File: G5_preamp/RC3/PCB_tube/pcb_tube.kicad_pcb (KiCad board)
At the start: 2 copper layers, 100 x 47 mm, 31 parts, among them J1 PSU_TUBE, J2 PCB_TUBE, J3 OT

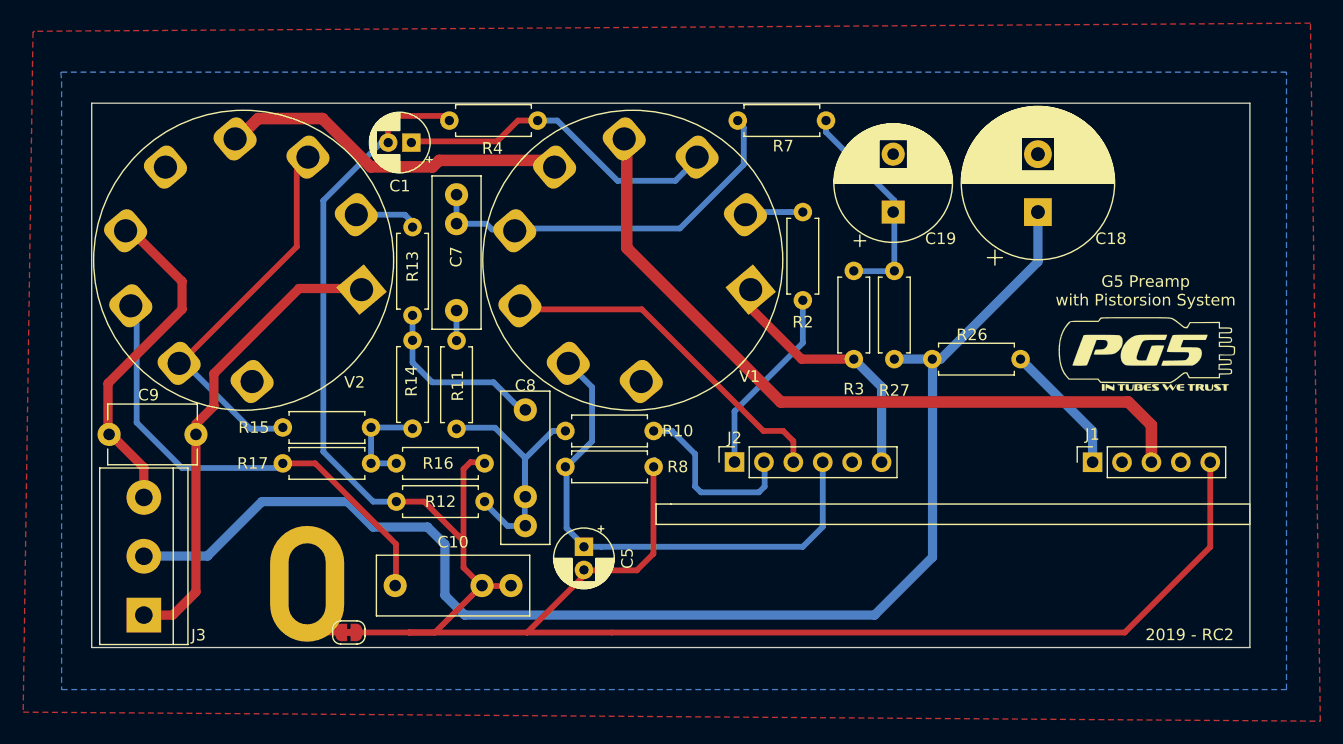
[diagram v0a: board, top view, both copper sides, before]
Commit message: RC3 update
Cathode Cap change 3d models and place (pcb-main)
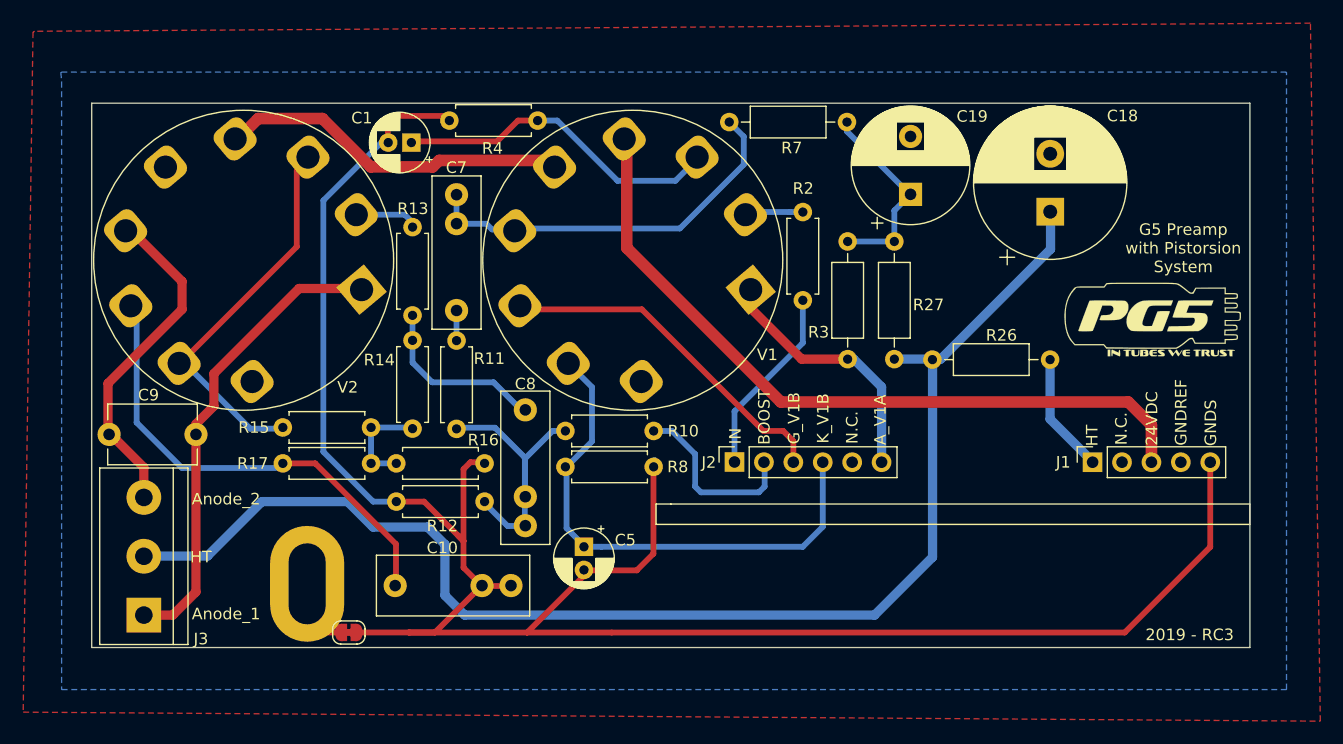
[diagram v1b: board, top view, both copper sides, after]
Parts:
- R26, R27, R3, R7: footprint Resistor_THT:R_Axial_DIN0207_L6.3mm_D2.5mm_P7.62mm_Horizontal -> Resistor_THT:R_Axial_DIN0207_L6.3mm_D2.5mm_P10.16mm_Horizontal
- moved REF** 3.01 mm to (121.6, 71.4)
- moved R3 2.59 mm to (95.3, 64.9)
- moved R26 2.55 mm to (112.8, 75.1)
- moved C19 2.14 mm to (100.7, 60.9)
- moved R7 1.81 mm to (95.2, 54.6)
- moved C18 1.06 mm to (112.8, 62.4)
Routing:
- net Net-(C19-Pad1): track 19.4 -> 17.2 mm
- net /HT2: track 11.5 -> 10.4 mm
- net /A+: track 115.9 -> 116.5 mm
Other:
- board text added: "2019 - RC3"
- board text added: "24VDC"
- board text added: "A_V1A"
- board text added: "Anode_1"
- board text added: "Anode_2"
- board text added: "BOOST"
- board text added: "GNDREF"
- board text added: "GNDS"
- board text added: "G_V1B"
- board text added: "HT"
- board text added: "IN"
- board text added: "K_V1B"
- board text added: "N.C."
- board text removed: "2019 - RC2"

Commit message: RC3 multivoltage
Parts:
- removed REF**: PG5_Logo_15mm_SilkScreen, Symbol:PG5_Logo_15mm_SilkScreen
- added J4: Conn_02x02_Odd_Even, Connector_PinHeader_2.54mm:PinHeader_1x04_P2.54mm_Vertical, F.Cu at (64.5, 56.5)
- added R20: 10k, Resistor_THT:R_Axial_DIN0207_L6.3mm_D2.5mm_P7.62mm_Horizontal, F.Cu at (81.8, 95.7)
- J2: footprint Connector_PinSocket_2.54mm:PinSocket_1x06_P2.54mm_Vertical -> Connector_PinHeader_2.54mm:PinHeader_1x07_P2.54mm_Vertical
- moved C1 38.3 mm to (95.9, 56.8), turned to 90 degrees
- moved R4 15.9 mm to (84.4, 54.8), turned to 0 degrees
- moved R7 7.64 mm to (100.6, 60.0)
- moved C19 6.21 mm to (106.9, 60.8)
- moved C18 6.18 mm to (118.9, 62.3)
- moved R26 1.15 mm to (113.9, 75.1)
- moved R2 0.73 mm to (91.5, 63.1)
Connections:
- C10 pad 2: GNDS -> /NFB
- J1 pad 2: Net-(J1-Pad2) -> (no net)
- J1 pad 3: /24VDC -> /HEATER
- J2 pad 5: Net-(J2-Pad5) -> /NFB
- J2 pad 6: /A_V1A -> (no net)
- R16 pad 2: GNDS -> /NFB
- V1 pad 4: /24VDC -> /HEATER1
- V1 pad 9: Net-(V1-Pad9) -> (no net)
- V2 pad 9: Net-(V2-Pad9) -> (no net)
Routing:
- net /HEATER: track 0.00 -> 76.2 mm
- net /24VDC: track 64.7 -> 0.00 mm
- net /NFB: track 0.00 -> 54.4 mm
- net /HEATER1: track 0.00 -> 16.1 mm
- net Net-(C1-Pad1): track 28.7 -> 16.5 mm
- net /A+: track 116.5 -> 122.0 mm
- net GNDS: track 181.6 -> 186.0 mm
- net /HEATER2: track 30.2 -> 33.8 mm
- net Net-(C8-Pad2): track 25.4 -> 21.9 mm
- net Net-(C19-Pad1): track 17.2 -> 16.1 mm
- net /IN: track 16.5 -> 15.8 mm
- net /A_V1A: track 22.4 -> 23.2 mm
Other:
- board text added: "24V 12V"
- board text added: "HEATER"
- board text added: "NFB"
- board text added: "or"
- board text removed: "24VDC"
